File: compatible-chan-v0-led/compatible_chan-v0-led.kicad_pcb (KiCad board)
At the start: 2 copper layers, 51 x 51 mm, 11 parts, among them J1 Conn_01x07_Pin, U1 MAX7219, U2 MAX7219

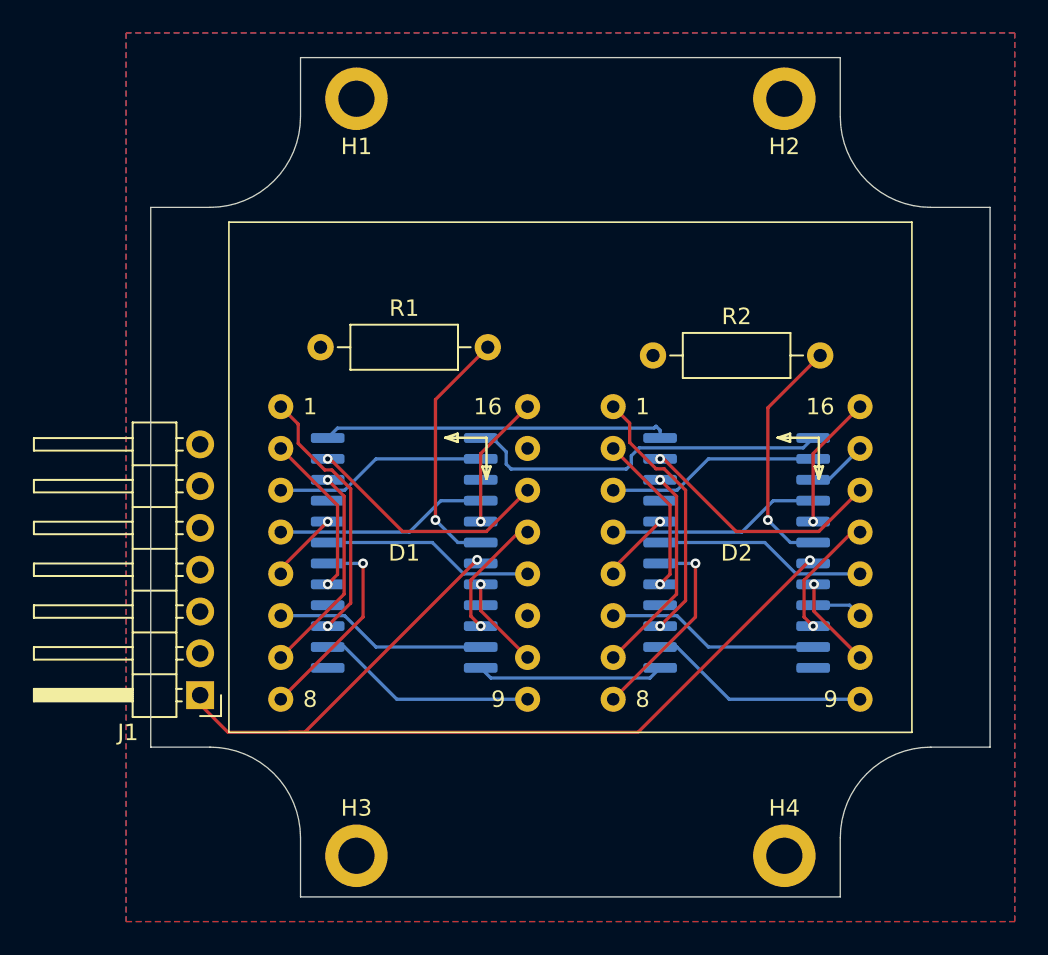
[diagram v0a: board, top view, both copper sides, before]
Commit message: LED版関連更新 基板更新,シェル設計
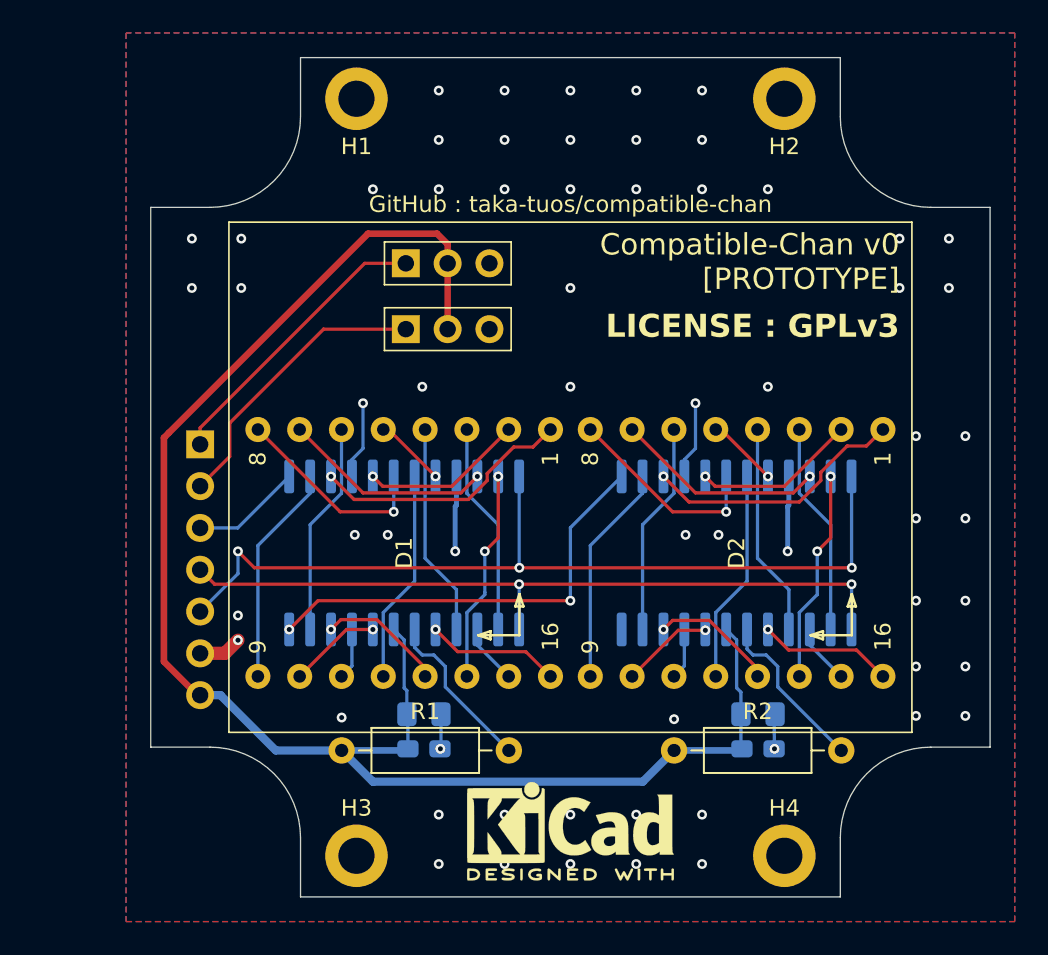
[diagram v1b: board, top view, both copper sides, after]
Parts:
- added C1: 100n, Capacitor_SMD:C_0805_2012Metric_Pad1.18x1.45mm_HandSolder, B.Cu at (86.1, 84.9)
- added C2: 100n, Capacitor_SMD:C_0805_2012Metric_Pad1.18x1.45mm_HandSolder, B.Cu at (106.4, 84.9)
- added C3: 10u, Capacitor_Tantalum_SMD:CP_EIA-2012-15_AVX-P_Pad1.30x1.05mm_HandSolder, B.Cu at (86.1, 87.0)
- added C4: 10u, Capacitor_Tantalum_SMD:CP_EIA-2012-15_AVX-P_Pad1.30x1.05mm_HandSolder, B.Cu at (106.4, 87.0)
- added J2: SERVO1, Connector_PinHeader_2.54mm:PinHeader_1x03_P2.54mm_Vertical, B.Cu at (85.0, 61.5)
- added J3: SERVO2, Connector_PinHeader_2.54mm:PinHeader_1x03_P2.54mm_Vertical, B.Cu at (85.0, 57.5)
- added REF**: KiCad-Logo2_5mm_SilkScreen, Symbol:KiCad-Logo2_5mm_SilkScreen, F.Cu at (95.0, 92.0)
- added REF**: OSHW-Logo2_14.6x12mm_SilkScreen, Symbol:OSHW-Logo2_14.6x12mm_SilkScreen, B.Cu at (107.4, 58.7)
- J1: value Conn_01x07_Pin -> EXT; moved to B.Cu
- moved R1 24.5 mm to (81.1, 87.1)
- moved R2 24.0 mm to (101.3, 87.1)
- moved J1 15.2 mm to (72.5, 68.5)
- turned D1 to -90 degrees
- turned D2 to -90 degrees
- turned U1 to -90 degrees
- turned U2 to -90 degrees
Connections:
- J1 pad 1: VCC -> SIG2
- J1 pad 2: GND -> SIG1
- J1 pad 3: LOAD -> DIN
- J1 pad 5: DIN -> LOAD
- J1 pad 6: SIG1 -> GND
- J1 pad 7: SIG2 -> VCC
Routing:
- net VCC: track 58.4 -> 100.3 mm, vias 2 -> 0
- net LOAD: track 21.1 -> 53.5 mm, vias 0 -> 3
- net GND: track 0.00 -> 25.5 mm, vias 0 -> 63
- net CLK: track 22.5 -> 46.2 mm, vias 0 -> 2
- net SIG1: track 0.00 -> 17.6 mm
- net SIG2: track 0.00 -> 17.6 mm
- net Net-(U1-DOUT): track 11.4 -> 26.7 mm, vias 0 -> 2
- net DIN: track 0.00 -> 7.68 mm
- net Net-(U1-ISET): track 15.1 -> 10.1 mm, vias 1 -> 0
- net Net-(U2-ISET): track 14.6 -> 10.2 mm, vias 1 -> 0
- net /D1.F: track 0.00 -> 3.64 mm
- net /D1.E: track 0.00 -> 3.11 mm
- net /D1.1: track 15.0 -> 12.9 mm, vias 1 -> 2
- net /D2.1: track 15.0 -> 12.9 mm, vias 1 -> 2
- added copper zone on B.Cu, net GND
- added copper zone on F.Cu, net GND
- removed copper zone on B.Cu, net (none)
- removed copper zone on F.Cu, net (none)
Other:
- board text added: "1 SIG2 2 SIG1 3 DIN 4 CLK 5 LOAD 6 GND 7 5V"
- board text added: "5V"
- board text added: "Compatible-Chan v0 [PROTOTYPE]"
- board text added: "GND"
- board text added: "GitHub : taka-tuos/compatible-chan"
- board text added: "LICENSE : GPLv3"
- board text added: "SERVO1"
- board text added: "SERVO2"
- board text added: "SIG"

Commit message: v0-led基板更新、テストファーム・v0.1用MCU基板追加
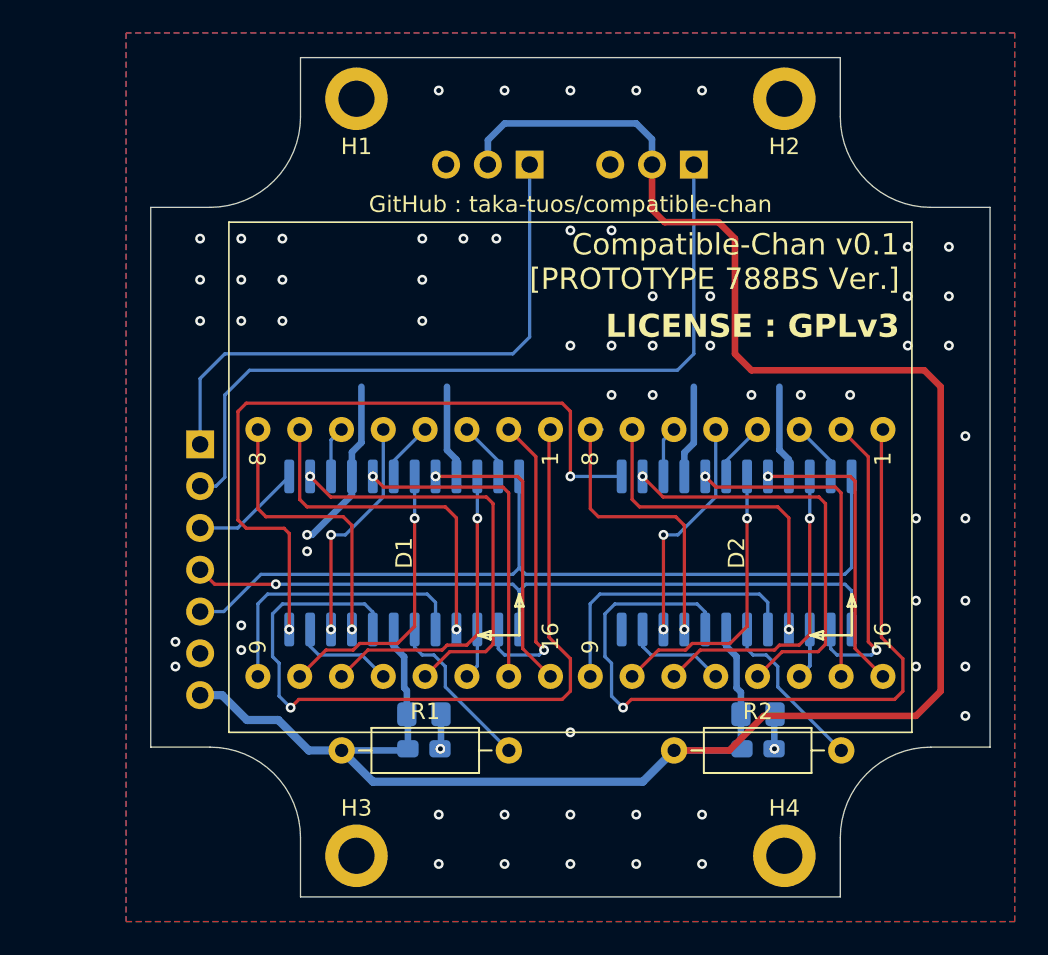
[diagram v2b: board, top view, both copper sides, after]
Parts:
- D1, D2: value 788AS -> 788BS
- REF**: moved to B.Cu
- moved REF** 33.1 mm to (93.0, 59.0), turned to 180 degrees
- moved J2 20.2 mm to (102.5, 51.5), turned to 90 degrees
- moved J3 9.62 mm to (92.5, 51.5), turned to 90 degrees
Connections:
- D1 pad 1: /D1.4 -> /D1.C
- D1 pad 10: /D1.C -> /D1.3
- D1 pad 11: /D1.E -> /D1.5
- D1 pad 12: /D1.3 -> /D1.D
- D1 pad 13: /D1.DP -> /D1.0
- D1 pad 14: /D1.1 -> /D1.F
- D1 pad 15: /D1.F -> /D1.6
- D1 pad 16: /D1.G -> /D1.7
- D1 pad 2: /D1.6 -> /D1.A
- D1 pad 3: /D1.A -> /D1.1
- D1 pad 4: /D1.B -> /D1.2
- D1 pad 5: /D1.7 -> /D1.DP
- D1 pad 6: /D1.D -> /D1.4
- D1 pad 7: /D1.5 -> /D1.B
- D1 pad 8: /D1.2 -> /D1.E
- D1 pad 9: /D1.0 -> /D1.G
- D2 pad 1: /D2.4 -> /D2.C
- D2 pad 10: /D2.C -> /D2.3
- D2 pad 11: /D2.E -> /D2.5
- D2 pad 12: /D2.3 -> /D2.D
- D2 pad 13: /D2.DP -> /D2.0
- D2 pad 14: /D2.1 -> /D2.F
- D2 pad 15: /D2.F -> /D2.6
- D2 pad 16: /D2.G -> /D2.7
- D2 pad 2: /D2.6 -> /D2.A
- D2 pad 3: /D2.A -> /D2.1
- D2 pad 4: /D2.B -> /D2.2
- D2 pad 5: /D2.7 -> /D2.DP
- D2 pad 6: /D2.D -> /D2.4
- D2 pad 7: /D2.5 -> /D2.B
- D2 pad 8: /D2.2 -> /D2.E
- D2 pad 9: /D2.0 -> /D2.G
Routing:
- net /D2.C: track 5.61 -> 47.6 mm
- net /D1.C: track 5.63 -> 47.6 mm
- net VCC: track 100.3 -> 134.8 mm
- net SIG1: track 17.6 -> 47.8 mm
- net SIG2: track 17.6 -> 35.5 mm
- net Net-(U1-DOUT): track 26.7 -> 43.6 mm
- net /D2.E: track 3.11 -> 18.0 mm, vias 0 -> 1
- net /D1.E: track 3.11 -> 17.3 mm, vias 0 -> 1
- net /D2.7: track 4.36 -> 18.0 mm
- net /D1.7: track 4.36 -> 18.0 mm
- net /D2.4: track 16.1 -> 3.11 mm, vias 1 -> 0
- net /D1.4: track 15.9 -> 3.11 mm, vias 1 -> 0
- net /D1.0: track 13.5 -> 25.8 mm, vias 0 -> 1
- net /D2.0: track 13.5 -> 25.8 mm, vias 0 -> 1
- net /D1.6: track 9.93 -> 19.8 mm
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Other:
- board text added: "Compatible-Chan v0.1 [PROTOTYPE 788BS Ver.]"
- board text removed: "Compatible-Chan v0 [PROTOTYPE]"
